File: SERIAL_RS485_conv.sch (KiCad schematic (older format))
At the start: 12 parts, among them P6 TB_IN, P7 TB_OUT, U5 ST3485EBDR, U6 ST3485EBDR

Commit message: Modified LAN9500A schematic.
Modified the schematic for the USB to Ethernet converter.
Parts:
- C48: renamed from C43; footprint Capacitors_SMD:C_0603_HandSoldering -> Capacitors_SMD:C_0805_HandSoldering
- C49: renamed from C44; footprint Capacitors_SMD:C_0603_HandSoldering -> Capacitors_SMD:C_0805_HandSoldering
- C50: renamed from C45; footprint Capacitors_SMD:C_0603_HandSoldering -> Capacitors_SMD:C_0805_HandSoldering
- C51: renamed from C46; footprint Capacitors_SMD:C_0603_HandSoldering -> Capacitors_SMD:C_0805_HandSoldering
- C52: renamed from C47; footprint Capacitors_SMD:C_0603_HandSoldering -> Capacitors_SMD:C_0805_HandSoldering
- C53: renamed from C48; footprint Capacitors_SMD:C_0603_HandSoldering -> Capacitors_SMD:C_0805_HandSoldering
- C54: renamed from C49; footprint Capacitors_SMD:C_0603_HandSoldering -> Capacitors_SMD:C_0805_HandSoldering
- C55: renamed from C50; footprint Capacitors_SMD:C_0603_HandSoldering -> Capacitors_SMD:C_0805_HandSoldering
- U5, U6: footprint Housings_SO8 -> (none)
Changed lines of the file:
@@
 F 0 "U5" H 3800 4400 50  0000 L CNN
 F 1 "ST3485EBDR" H 4200 4400 50  0000 L CNN
-F 2 "Housings_SO8" H 4450 3700 50  0001 C CIN
+F 2 "" H 4450 3700 50  0001 C CIN
 F 3 "" H 4100 4050 50  0000 C CNN
 	1    4100 4050
@@
 F 0 "U6" H 6750 4400 50  0000 L CNN
 F 1 "ST3485EBDR" H 7150 4400 50  0000 L CNN
-F 2 "Housings_SO8" H 7400 3700 50  0001 C CIN
+F 2 "" H 7400 3700 50  0001 C CIN
 F 3 "" H 7050 4050 50  0000 C CNN
 	1    7050 4050
@@
 $EndComp
 $Comp
-L +3.3V #PWR074
+L +3.3V #PWR079
 U 1 1 588FE7B3
 P 4100 3100
-F 0 "#PWR074" H 4100 2950 50  0001 C CNN
+F 0 "#PWR079" H 4100 2950 50  0001 C CNN
 F 1 "+3.3V" H 4100 3240 50  0000 C CNN
 F 2 "" H 4100 3100 50  0000 C CNN
@@
 $EndComp
 $Comp
-L C C45
+L C C50
 U 1 1 588FE822
 P 4350 3200
-F 0 "C45" V 4300 3300 50  0000 L CNN
+F 0 "C50" V 4300 3300 50  0000 L CNN
 F 1 "1uF" V 4200 3150 50  0000 L CNN
-F 2 "Capacitors_SMD:C_0603_HandSoldering" H 4388 3050 50  0001 C CNN
+F 2 "Capacitors_SMD:C_0805_HandSoldering" H 4388 3050 50  0001 C CNN
 F 3 "" H 4350 3200 50  0000 C CNN
 	1    4350 3200
@@
 $EndComp
 $Comp
-L C C46
+L C C51
 U 1 1 588FE88A
 P 4350 3500
-F 0 "C46" V 4400 3600 50  0000 L CNN
+F 0 "C51" V 4400 3600 50  0000 L CNN
 F 1 "100nF" V 4200 3400 50  0000 L CNN
-F 2 "Capacitors_SMD:C_0603_HandSoldering" H 4388 3350 50  0001 C CNN
+F 2 "Capacitors_SMD:C_0805_HandSoldering" H 4388 3350 50  0001 C CNN
 F 3 "" H 4350 3500 50  0000 C CNN
 	1    4350 3500
@@
 $EndComp
 $Comp
-L GND #PWR075
+L GND #PWR080
 U 1 1 588FEA04
 P 4600 3350
-F 0 "#PWR075" H 4600 3100 50  0001 C CNN
+F 0 "#PWR080" H 4600 3100 50  0001 C CNN
 F 1 "GND" H 4600 3200 50  0000 C CNN
 F 2 "" H 4600 3350 50  0000 C CNN
@@
 Connection ~ 4550 3350
 $Comp
-L +3.3V #PWR076
+L +3.3V #PWR081
 U 1 1 588FEB3E
 P 7050 3100
-F 0 "#PWR076" H 7050 2950 50  0001 C CNN
+F 0 "#PWR081" H 7050 2950 50  0001 C CNN
 F 1 "+3.3V" H 7050 3240 50  0000 C CNN
 F 2 "" H 7050 3100 50  0000 C CNN
@@
 $EndComp
 $Comp
-L C C49
+L C C54
 U 1 1 588FEB44
 P 7300 3200
-F 0 "C49" V 7250 3300 50  0000 L CNN
+F 0 "C54" V 7250 3300 50  0000 L CNN
 F 1 "1uF" V 7150 3150 50  0000 L CNN
-F 2 "Capacitors_SMD:C_0603_HandSoldering" H 7338 3050 50  0001 C CNN
+F 2 "Capacitors_SMD:C_0805_HandSoldering" H 7338 3050 50  0001 C CNN
 F 3 "" H 7300 3200 50  0000 C CNN
 	1    7300 3200
@@
 $EndComp
 $Comp
-L C C50
+L C C55
 U 1 1 588FEB4A
 P 7300 3500
-F 0 "C50" V 7350 3600 50  0000 L CNN
+F 0 "C55" V 7350 3600 50  0000 L CNN
 F 1 "100nF" V 7150 3400 50  0000 L CNN
-F 2 "Capacitors_SMD:C_0603_HandSoldering" H 7338 3350 50  0001 C CNN
+F 2 "Capacitors_SMD:C_0805_HandSoldering" H 7338 3350 50  0001 C CNN
 F 3 "" H 7300 3500 50  0000 C CNN
 	1    7300 3500
@@
 $EndComp
 $Comp
-L GND #PWR077
+L GND #PWR082
 U 1 1 588FEB50
 P 7550 3350
-F 0 "#PWR077" H 7550 3100 50  0001 C CNN
+F 0 "#PWR082" H 7550 3100 50  0001 C CNN
 F 1 "GND" H 7550 3200 50  0000 C CNN
 F 2 "" H 7550 3350 50  0000 C CNN
@@
 	4550 4100 4600 4100
 $Comp
-L GND #PWR078
+L GND #PWR083
 U 1 1 588FEED7
 P 4100 4550
-F 0 "#PWR078" H 4100 4300 50  0001 C CNN
+F 0 "#PWR083" H 4100 4300 50  0001 C CNN
 F 1 "GND" H 4100 4400 50  0000 C CNN
 F 2 "" H 4100 4550 50  0000 C CNN
@@
 $EndComp
 $Comp
-L GND #PWR079
+L GND #PWR084
 U 1 1 588FEEFA
 P 7050 4550
-F 0 "#PWR079" H 7050 4300 50  0001 C CNN
+F 0 "#PWR084" H 7050 4300 50  0001 C CNN
 F 1 "GND" H 7050 4400 50  0000 C CNN
 F 2 "" H 7050 4550 50  0000 C CNN
@@
 	4100 4550 4100 4450
 $Comp
-L +3.3V #PWR080
+L +3.3V #PWR085
 U 1 1 588FF500
 P 2850 4150
-F 0 "#PWR080" H 2850 4000 50  0001 C CNN
+F 0 "#PWR085" H 2850 4000 50  0001 C CNN
 F 1 "+3.3V" H 2850 4290 50  0000 C CNN
 F 2 "" H 2850 4150 50  0000 C CNN
@@
 $EndComp
 $Comp
-L C C44
+L C C49
 U 1 1 588FF506
 P 3300 4400
-F 0 "C44" H 3150 4550 50  0000 L CNN
+F 0 "C49" H 3150 4550 50  0000 L CNN
 F 1 "1uF" H 3050 4400 50  0000 L CNN
-F 2 "Capacitors_SMD:C_0603_HandSoldering" H 3338 4250 50  0001 C CNN
+F 2 "Capacitors_SMD:C_0805_HandSoldering" H 3338 4250 50  0001 C CNN
 F 3 "" H 3300 4400 50  0000 C CNN
 	1    3300 4400
@@
 $EndComp
 $Comp
-L C C43
+L C C48
 U 1 1 588FF50C
 P 3000 4400
-F 0 "C43" H 3025 4500 50  0000 L CNN
+F 0 "C48" H 3025 4500 50  0000 L CNN
 F 1 "100nF" H 3050 4300 50  0000 L CNN
-F 2 "Capacitors_SMD:C_0603_HandSoldering" H 3038 4250 50  0001 C CNN
+F 2 "Capacitors_SMD:C_0805_HandSoldering" H 3038 4250 50  0001 C CNN
 F 3 "" H 3000 4400 50  0000 C CNN
 	1    3000 4400
@@
 $EndComp
 $Comp
-L GND #PWR081
+L GND #PWR086
 U 1 1 588FF512
 P 3150 4650
-F 0 "#PWR081" H 3150 4400 50  0001 C CNN
+F 0 "#PWR086" H 3150 4400 50  0001 C CNN
 F 1 "GND" H 3150 4500 50  0000 C CNN
 F 2 "" H 3150 4650 50  0000 C CNN
@@
 	3600 4250 3700 4250
 $Comp
-L GND #PWR082
+L GND #PWR087
 U 1 1 588FFA34
 P 3600 3950
-F 0 "#PWR082" H 3600 3700 50  0001 C CNN
+F 0 "#PWR087" H 3600 3700 50  0001 C CNN
 F 1 "GND" H 3600 3800 50  0000 C CNN
 F 2 "" H 3600 3950 50  0000 C CNN
@@
 	3600 3950 3700 3950
 $Comp
-L GND #PWR083
+L GND #PWR088
 U 1 1 588FFC3B
 P 6550 3950
-F 0 "#PWR083" H 6550 3700 50  0001 C CNN
+F 0 "#PWR088" H 6550 3700 50  0001 C CNN
 F 1 "GND" H 6550 3800 50  0000 C CNN
 F 2 "" H 6550 3950 50  0000 C CNN
@@
 DI_OUT
 $Comp
-L +3.3V #PWR084
+L +3.3V #PWR089
 U 1 1 588FFF45
 P 5800 4150
-F 0 "#PWR084" H 5800 4000 50  0001 C CNN
+F 0 "#PWR089" H 5800 4000 50  0001 C CNN
 F 1 "+3.3V" H 5800 4290 50  0000 C CNN
 F 2 "" H 5800 4150 50  0000 C CNN
@@
 $EndComp
 $Comp
-L C C48
+L C C53
 U 1 1 588FFF4B
 P 6250 4400
-F 0 "C48" H 6050 4500 50  0000 L CNN
+F 0 "C53" H 6050 4500 50  0000 L CNN
 F 1 "1uF" H 6000 4350 50  0000 L CNN
-F 2 "Capacitors_SMD:C_0603_HandSoldering" H 6288 4250 50  0001 C CNN
+F 2 "Capacitors_SMD:C_0805_HandSoldering" H 6288 4250 50  0001 C CNN
 F 3 "" H 6250 4400 50  0000 C CNN
 	1    6250 4400
@@
 $EndComp
 $Comp
-L C C47
+L C C52
 U 1 1 588FFF51
 P 5950 4400
-F 0 "C47" H 5975 4500 50  0000 L CNN
+F 0 "C52" H 5975 4500 50  0000 L CNN
 F 1 "100nF" H 6100 4400 50  0000 L CNN
-F 2 "Capacitors_SMD:C_0603_HandSoldering" H 5988 4250 50  0001 C CNN
+F 2 "Capacitors_SMD:C_0805_HandSoldering" H 5988 4250 50  0001 C CNN
 F 3 "" H 5950 4400 50  0000 C CNN
 	1    5950 4400
@@
 $EndComp
 $Comp
-L GND #PWR085
+L GND #PWR090
 U 1 1 588FFF57
 P 6100 4650
-F 0 "#PWR085" H 6100 4400 50  0001 C CNN
+F 0 "#PWR090" H 6100 4400 50  0001 C CNN
 F 1 "GND" H 6100 4500 50  0000 C CNN
 F 2 "" H 6100 4650 50  0000 C CNN

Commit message: Schematic changes. PCB in process of making.
Removed LAN9500A Jtag. Removed Aria G25 pinout. Removed USB connectors. Added rezistors to USB/ETH/ySD shields.
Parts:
- P6, P7: footprint (none) -> Connectors_Terminal_Blocks:TerminalBlock_Pheonix_PT-3.5mm_2pol
- U5, U6: footprint (none) -> Power_Integrations:SO-8
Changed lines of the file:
@@
 $Descr A4 11693 8268
 encoding utf-8
-Sheet 6 7
+Sheet 7 7
 Title ""
 Date ""
@@
 F 0 "U5" H 3800 4400 50  0000 L CNN
 F 1 "ST3485EBDR" H 4200 4400 50  0000 L CNN
-F 2 "" H 4450 3700 50  0001 C CIN
+F 2 "Power_Integrations:SO-8" H 4450 3700 50  0001 C CIN
 F 3 "" H 4100 4050 50  0000 C CNN
 	1    4100 4050
@@
 F 0 "U6" H 6750 4400 50  0000 L CNN
 F 1 "ST3485EBDR" H 7150 4400 50  0000 L CNN
-F 2 "" H 7400 3700 50  0001 C CIN
+F 2 "Power_Integrations:SO-8" H 7400 3700 50  0001 C CIN
 F 3 "" H 7050 4050 50  0000 C CNN
 	1    7050 4050
@@
 $EndComp
 $Comp
-L +3.3V #PWR079
+L +3.3V #PWR069
 U 1 1 588FE7B3
 P 4100 3100
-F 0 "#PWR079" H 4100 2950 50  0001 C CNN
+F 0 "#PWR069" H 4100 2950 50  0001 C CNN
 F 1 "+3.3V" H 4100 3240 50  0000 C CNN
 F 2 "" H 4100 3100 50  0000 C CNN
@@
 $EndComp
 $Comp
-L GND #PWR080
+L GND #PWR070
 U 1 1 588FEA04
 P 4600 3350
-F 0 "#PWR080" H 4600 3100 50  0001 C CNN
+F 0 "#PWR070" H 4600 3100 50  0001 C CNN
 F 1 "GND" H 4600 3200 50  0000 C CNN
 F 2 "" H 4600 3350 50  0000 C CNN
@@
 Connection ~ 4550 3350
 $Comp
-L +3.3V #PWR081
+L +3.3V #PWR071
 U 1 1 588FEB3E
 P 7050 3100
-F 0 "#PWR081" H 7050 2950 50  0001 C CNN
+F 0 "#PWR071" H 7050 2950 50  0001 C CNN
 F 1 "+3.3V" H 7050 3240 50  0000 C CNN
 F 2 "" H 7050 3100 50  0000 C CNN
@@
 $EndComp
 $Comp
-L GND #PWR082
+L GND #PWR072
 U 1 1 588FEB50
 P 7550 3350
-F 0 "#PWR082" H 7550 3100 50  0001 C CNN
+F 0 "#PWR072" H 7550 3100 50  0001 C CNN
 F 1 "GND" H 7550 3200 50  0000 C CNN
 F 2 "" H 7550 3350 50  0000 C CNN
@@
 F 0 "P7" H 7750 4200 50  0000 C CNN
 F 1 "TB_OUT" V 7850 4050 50  0000 C CNN
-F 2 "" H 7750 4050 50  0001 C CNN
+F 2 "Connectors_Terminal_Blocks:TerminalBlock_Pheonix_PT-3.5mm_2pol" H 7750 4050 50  0001 C CNN
 F 3 "" H 7750 4050 50  0000 C CNN
 	1    7750 4050
@@
 F 0 "P6" H 4800 4200 50  0000 C CNN
 F 1 "TB_IN" V 4900 4050 50  0000 C CNN
-F 2 "" H 4800 4050 50  0001 C CNN
+F 2 "Connectors_Terminal_Blocks:TerminalBlock_Pheonix_PT-3.5mm_2pol" H 4800 4050 50  0001 C CNN
 F 3 "" H 4800 4050 50  0000 C CNN
 	1    4800 4050
@@
 	4550 4100 4600 4100
 $Comp
-L GND #PWR083
+L GND #PWR073
 U 1 1 588FEED7
 P 4100 4550
-F 0 "#PWR083" H 4100 4300 50  0001 C CNN
+F 0 "#PWR073" H 4100 4300 50  0001 C CNN
 F 1 "GND" H 4100 4400 50  0000 C CNN
 F 2 "" H 4100 4550 50  0000 C CNN
@@
 $EndComp
 $Comp
-L GND #PWR084
+L GND #PWR074
 U 1 1 588FEEFA
 P 7050 4550
-F 0 "#PWR084" H 7050 4300 50  0001 C CNN
+F 0 "#PWR074" H 7050 4300 50  0001 C CNN
 F 1 "GND" H 7050 4400 50  0000 C CNN
 F 2 "" H 7050 4550 50  0000 C CNN
@@
 	4100 4550 4100 4450
 $Comp
-L +3.3V #PWR085
+L +3.3V #PWR075
 U 1 1 588FF500
 P 2850 4150
-F 0 "#PWR085" H 2850 4000 50  0001 C CNN
+F 0 "#PWR075" H 2850 4000 50  0001 C CNN
 F 1 "+3.3V" H 2850 4290 50  0000 C CNN
 F 2 "" H 2850 4150 50  0000 C CNN
@@
 $EndComp
 $Comp
-L GND #PWR086
+L GND #PWR076
 U 1 1 588FF512
 P 3150 4650
-F 0 "#PWR086" H 3150 4400 50  0001 C CNN
+F 0 "#PWR076" H 3150 4400 50  0001 C CNN
 F 1 "GND" H 3150 4500 50  0000 C CNN
 F 2 "" H 3150 4650 50  0000 C CNN
@@
 	3600 4250 3700 4250
 $Comp
-L GND #PWR087
+L GND #PWR077
 U 1 1 588FFA34
 P 3600 3950
-F 0 "#PWR087" H 3600 3700 50  0001 C CNN
+F 0 "#PWR077" H 3600 3700 50  0001 C CNN
 F 1 "GND" H 3600 3800 50  0000 C CNN
 F 2 "" H 3600 3950 50  0000 C CNN
@@
 	3600 3950 3700 3950
 $Comp
-L GND #PWR088
+L GND #PWR078
 U 1 1 588FFC3B
 P 6550 3950
-F 0 "#PWR088" H 6550 3700 50  0001 C CNN
+F 0 "#PWR078" H 6550 3700 50  0001 C CNN
 F 1 "GND" H 6550 3800 50  0000 C CNN
 F 2 "" H 6550 3950 50  0000 C CNN
@@
 DI_OUT
 $Comp
-L +3.3V #PWR089
+L +3.3V #PWR079
 U 1 1 588FFF45
 P 5800 4150
-F 0 "#PWR089" H 5800 4000 50  0001 C CNN
+F 0 "#PWR079" H 5800 4000 50  0001 C CNN
 F 1 "+3.3V" H 5800 4290 50  0000 C CNN
 F 2 "" H 5800 4150 50  0000 C CNN
@@
 $EndComp
 $Comp
-L GND #PWR090
+L GND #PWR080
 U 1 1 588FFF57
 P 6100 4650
-F 0 "#PWR090" H 6100 4400 50  0001 C CNN
+F 0 "#PWR080" H 6100 4400 50  0001 C CNN
 F 1 "GND" H 6100 4500 50  0000 C CNN
 F 2 "" H 6100 4650 50  0000 C CNN

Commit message: Modified buck circuit on board.
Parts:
- C48, C49, C50, C51, C52, C53, C54, C55: footprint Capacitors_SMD:C_0805_HandSoldering -> Capacitors_SMD:C_0603_HandSoldering
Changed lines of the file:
@@
 F 0 "C50" V 4300 3300 50  0000 L CNN
 F 1 "1uF" V 4200 3150 50  0000 L CNN
-F 2 "Capacitors_SMD:C_0805_HandSoldering" H 4388 3050 50  0001 C CNN
+F 2 "Capacitors_SMD:C_0603_HandSoldering" H 4388 3050 50  0001 C CNN
 F 3 "" H 4350 3200 50  0000 C CNN
 	1    4350 3200
@@
 F 0 "C51" V 4400 3600 50  0000 L CNN
 F 1 "100nF" V 4200 3400 50  0000 L CNN
-F 2 "Capacitors_SMD:C_0805_HandSoldering" H 4388 3350 50  0001 C CNN
+F 2 "Capacitors_SMD:C_0603_HandSoldering" H 4388 3350 50  0001 C CNN
 F 3 "" H 4350 3500 50  0000 C CNN
 	1    4350 3500
@@
 F 0 "C54" V 7250 3300 50  0000 L CNN
 F 1 "1uF" V 7150 3150 50  0000 L CNN
-F 2 "Capacitors_SMD:C_0805_HandSoldering" H 7338 3050 50  0001 C CNN
+F 2 "Capacitors_SMD:C_0603_HandSoldering" H 7338 3050 50  0001 C CNN
 F 3 "" H 7300 3200 50  0000 C CNN
 	1    7300 3200
@@
 F 0 "C55" V 7350 3600 50  0000 L CNN
 F 1 "100nF" V 7150 3400 50  0000 L CNN
-F 2 "Capacitors_SMD:C_0805_HandSoldering" H 7338 3350 50  0001 C CNN
+F 2 "Capacitors_SMD:C_0603_HandSoldering" H 7338 3350 50  0001 C CNN
 F 3 "" H 7300 3500 50  0000 C CNN
 	1    7300 3500
@@
 F 0 "C49" H 3150 4550 50  0000 L CNN
 F 1 "1uF" H 3050 4400 50  0000 L CNN
-F 2 "Capacitors_SMD:C_0805_HandSoldering" H 3338 4250 50  0001 C CNN
+F 2 "Capacitors_SMD:C_0603_HandSoldering" H 3338 4250 50  0001 C CNN
 F 3 "" H 3300 4400 50  0000 C CNN
 	1    3300 4400
@@
 F 0 "C48" H 3025 4500 50  0000 L CNN
 F 1 "100nF" H 3050 4300 50  0000 L CNN
-F 2 "Capacitors_SMD:C_0805_HandSoldering" H 3038 4250 50  0001 C CNN
+F 2 "Capacitors_SMD:C_0603_HandSoldering" H 3038 4250 50  0001 C CNN
 F 3 "" H 3000 4400 50  0000 C CNN
 	1    3000 4400
@@
 F 0 "C53" H 6050 4500 50  0000 L CNN
 F 1 "1uF" H 6000 4350 50  0000 L CNN
-F 2 "Capacitors_SMD:C_0805_HandSoldering" H 6288 4250 50  0001 C CNN
+F 2 "Capacitors_SMD:C_0603_HandSoldering" H 6288 4250 50  0001 C CNN
 F 3 "" H 6250 4400 50  0000 C CNN
 	1    6250 4400
@@
 F 0 "C52" H 5975 4500 50  0000 L CNN
 F 1 "100nF" H 6100 4400 50  0000 L CNN
-F 2 "Capacitors_SMD:C_0805_HandSoldering" H 5988 4250 50  0001 C CNN
+F 2 "Capacitors_SMD:C_0603_HandSoldering" H 5988 4250 50  0001 C CNN
 F 3 "" H 5950 4400 50  0000 C CNN
 	1    5950 4400

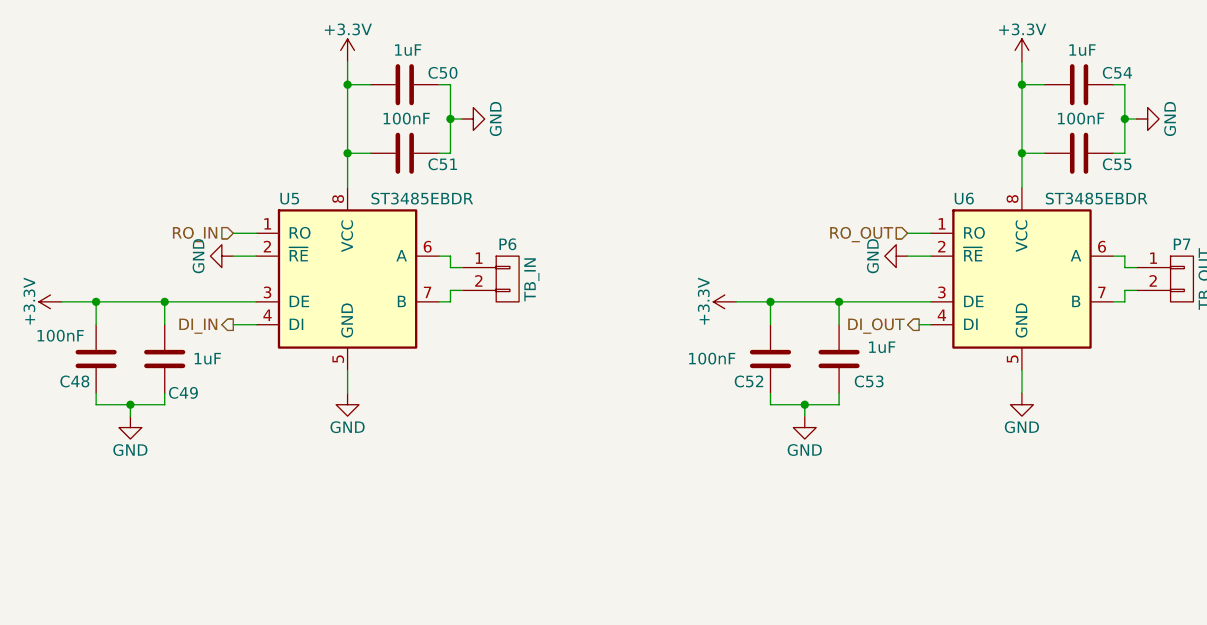
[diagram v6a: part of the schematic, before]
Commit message: Removed some capacitors.
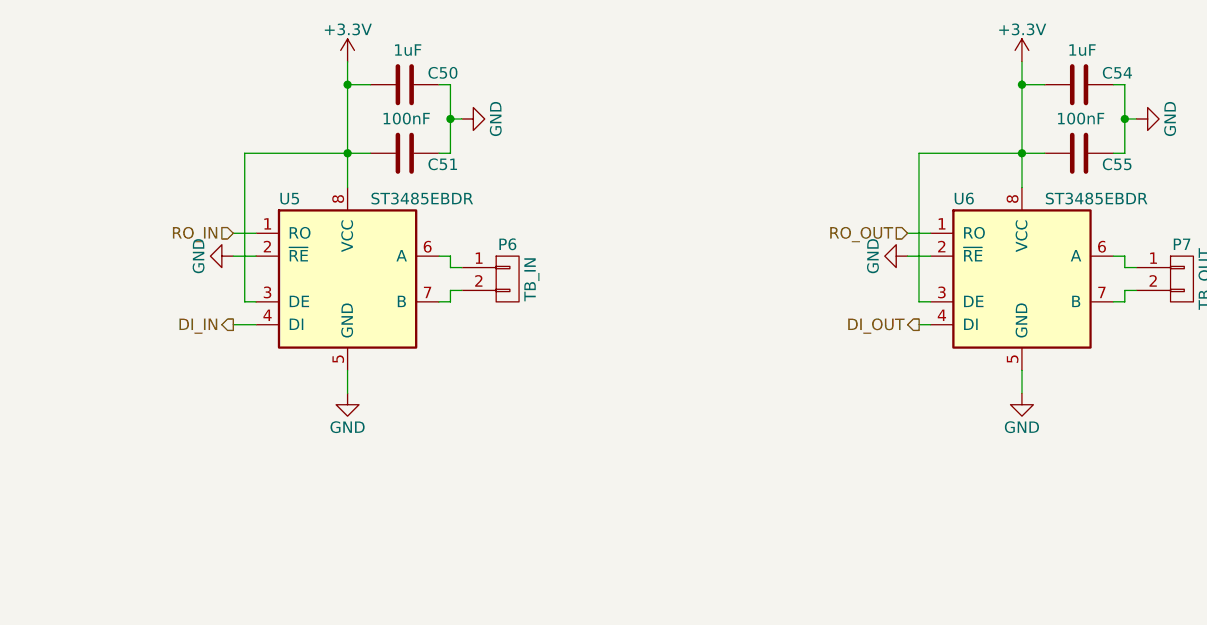
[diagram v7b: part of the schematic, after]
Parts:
- removed C48, C52: 100nF, Capacitors_SMD:C_0603_HandSoldering, symbol C
- removed C49, C53: 1uF, Capacitors_SMD:C_0603_HandSoldering, symbol C
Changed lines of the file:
@@
 	4100 3200 4200 3200
 Wire Wire Line
-	4100 3500 4200 3500
+	3650 3500 4200 3500
 Connection ~ 4100 3200
 Connection ~ 4100 3500
@@
 	7050 3200 7150 3200
 Wire Wire Line
-	7050 3500 7150 3500
+	6600 3500 7150 3500
 Connection ~ 7050 3200
 Connection ~ 7050 3500
@@
 Wire Wire Line
 	4100 4550 4100 4450
-$Comp
-L +3.3V #PWR074
-U 1 1 588FF500
-P 2850 4150
-F 0 "#PWR074" H 2850 4000 50  0001 C CNN
-F 1 "+3.3V" H 2850 4290 50  0000 C CNN
-F 2 "" H 2850 4150 50  0000 C CNN
-F 3 "" H 2850 4150 50  0000 C CNN
-	1    2850 4150
-	0    -1   -1   0
-$EndComp
-$Comp
-L C C49
-U 1 1 588FF506
-P 3300 4400
-F 0 "C49" H 3150 4550 50  0000 L CNN
-F 1 "1uF" H 3050 4400 50  0000 L CNN
-F 2 "Capacitors_SMD:C_0603_HandSoldering" H 3338 4250 50  0001 C CNN
-F 3 "" H 3300 4400 50  0000 C CNN
-	1    3300 4400
-	-1   0    0    1
-$EndComp
-$Comp
-L C C48
-U 1 1 588FF50C
-P 3000 4400
-F 0 "C48" H 3025 4500 50  0000 L CNN
-F 1 "100nF" H 3050 4300 50  0000 L CNN
-F 2 "Capacitors_SMD:C_0603_HandSoldering" H 3038 4250 50  0001 C CNN
-F 3 "" H 3000 4400 50  0000 C CNN
-	1    3000 4400
-	-1   0    0    1
-$EndComp
-$Comp
-L GND #PWR075
-U 1 1 588FF512
-P 3150 4650
-F 0 "#PWR075" H 3150 4400 50  0001 C CNN
-F 1 "GND" H 3150 4500 50  0000 C CNN
-F 2 "" H 3150 4650 50  0000 C CNN
-F 3 "" H 3150 4650 50  0000 C CNN
-	1    3150 4650
-	1    0    0    -1
-$EndComp
-Wire Wire Line
-	3300 4150 3300 4250
-Wire Wire Line
-	3000 4150 3000 4250
-Connection ~ 3300 4150
-Connection ~ 3000 4150
-Wire Wire Line
-	3150 4650 3150 4600
-Wire Wire Line
-	3300 4600 3000 4600
-Wire Wire Line
-	3300 4600 3300 4550
-Wire Wire Line
-	3000 4600 3000 4550
-Connection ~ 3150 4600
-Wire Wire Line
-	2850 4150 3700 4150
 Text HLabel 3600 4250 0    50   Output ~ 0
 DI_IN
@@
 Text HLabel 6550 3850 0    50   Input ~ 0
 RO_OUT
-Text HLabel 6600 4250 0    50   Output ~ 0
-DI_OUT
-$Comp
-L +3.3V #PWR078
-U 1 1 588FFF45
-P 5800 4150
-F 0 "#PWR078" H 5800 4000 50  0001 C CNN
-F 1 "+3.3V" H 5800 4290 50  0000 C CNN
-F 2 "" H 5800 4150 50  0000 C CNN
-F 3 "" H 5800 4150 50  0000 C CNN
-	1    5800 4150
-	0    -1   -1   0
-$EndComp
-$Comp
-L C C53
-U 1 1 588FFF4B
-P 6250 4400
-F 0 "C53" H 6050 4500 50  0000 L CNN
-F 1 "1uF" H 6000 4350 50  0000 L CNN
-F 2 "Capacitors_SMD:C_0603_HandSoldering" H 6288 4250 50  0001 C CNN
-F 3 "" H 6250 4400 50  0000 C CNN
-	1    6250 4400
-	-1   0    0    1
-$EndComp
-$Comp
-L C C52
-U 1 1 588FFF51
-P 5950 4400
-F 0 "C52" H 5975 4500 50  0000 L CNN
-F 1 "100nF" H 6100 4400 50  0000 L CNN
-F 2 "Capacitors_SMD:C_0603_HandSoldering" H 5988 4250 50  0001 C CNN
-F 3 "" H 5950 4400 50  0000 C CNN
-	1    5950 4400
-	-1   0    0    1
-$EndComp
-$Comp
-L GND #PWR079
-U 1 1 588FFF57
-P 6100 4650
-F 0 "#PWR079" H 6100 4400 50  0001 C CNN
-F 1 "GND" H 6100 4500 50  0000 C CNN
-F 2 "" H 6100 4650 50  0000 C CNN
-F 3 "" H 6100 4650 50  0000 C CNN
-	1    6100 4650
-	1    0    0    -1
-$EndComp
-Wire Wire Line
-	6250 4150 6250 4250
-Wire Wire Line
-	5950 4150 5950 4250
-Connection ~ 6250 4150
-Connection ~ 5950 4150
-Wire Wire Line
-	6100 4650 6100 4600
-Wire Wire Line
-	6250 4600 5950 4600
-Wire Wire Line
-	6250 4600 6250 4550
-Wire Wire Line
-	5950 4600 5950 4550
-Connection ~ 6100 4600
-Wire Wire Line
-	5800 4150 6650 4150
 Wire Wire Line
 	6600 4250 6650 4250
@@
 Wire Wire Line
 	6550 3850 6650 3850
+Wire Wire Line
+	3700 4150 3650 4150
+Wire Wire Line
+	3650 4150 3650 3500
+Text HLabel 6600 4250 0    50   Output ~ 0
+DI_OUT
+Wire Wire Line
+	6650 4150 6600 4150
+Wire Wire Line
+	6600 4150 6600 3500
 $EndSCHEMATC

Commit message: Modified schematic. v1.1
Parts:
- removed P6: TB_IN, Connectors_Terminal_Blocks:TerminalBlock_Pheonix_PT-3.5mm_2pol, symbol CONN_01X02
- removed P7: TB_OUT, Connectors_Terminal_Blocks:TerminalBlock_Pheonix_PT-3.5mm_2pol, symbol CONN_01X02
- added D10, D11, D12, D13, D14, D15: D_TVS, Diodes_SMD:D_SMA-SMB_Universal_Handsoldering, symbol D_TVS
- added J4, J5: Screw_Terminal_1x03, Connectors_Terminal_Blocks:TerminalBlock_Pheonix_PT-3.5mm_3pol, symbol Screw_Terminal_1x03
- added JP1, JP2, JP3, JP4, JP5, JP6: Jumper_NO_Small, Pin_Headers:Pin_Header_Straight_1x02_Pitch2.54mm, symbol Jumper_NO_Small
- added R36, R37, R38, R39, R40, R41: R, Resistors_SMD:R_0603_HandSoldering, symbol R
- renumbered C50 to C68, C51 to C69, C54 to C70, C55 to C71, U5 to U6, U6 to U7
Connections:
- net +3V3: now also D10.1 (A1), D13.1 (A1), R36.1, R39.1; no longer U6.3 (DE), U7.3 (DE)
- net GND: now also D12.2 (A2), D15.2 (A2), J4.1, J5.1, JP3.2, JP6.2; no longer U6.2 (~RE~), U7.2 (~RE~)
- net at U6.6 (A): now also D10.2 (A2), D11.1 (A1), J4.3, JP1.2, R37.1
- net at U6.7 (B): now also D11.2 (A2), D12.1 (A1), J4.2, JP2.2, R38.1
- net at U7.6 (A): now also D13.2 (A2), D14.1 (A1), J5.3, JP4.2, R40.1
- net at U7.7 (B): now also D14.2 (A2), D15.1 (A1), J5.2, JP5.2, R41.1
- net DI_IN renamed IN_DI
- net DI_OUT renamed OUT_DI
- net RO_IN renamed IN_RO
- net RO_OUT renamed OUT_RO
- new net: JP3.1, R38.2
- new net: JP2.1, R37.2
- new net: JP1.1, R36.2
- new net: JP6.1, R41.2
- new net: JP5.1, R40.2
- new net: JP4.1, R39.2
- new net IN_RTS: U6.2 (~RE~), U6.3 (DE)
- new net OUT_RTS: U7.2 (~RE~), U7.3 (DE)
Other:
- note removed: "RO is enabled when RE is low."
- note removed: "ST3485"
- note removed: "The driver outputs are enabled by bringing DE high."
- moved on the sheet: C68, C69, C70, C71, U6, U7
